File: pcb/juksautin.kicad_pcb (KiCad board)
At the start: 2 copper layers, 65 x 35 mm, 18 parts, among them J1 Screw_Terminal_01x09, J2 ATMEGA32U4 pin 42, U1 SP3485CN, U2 LM4041

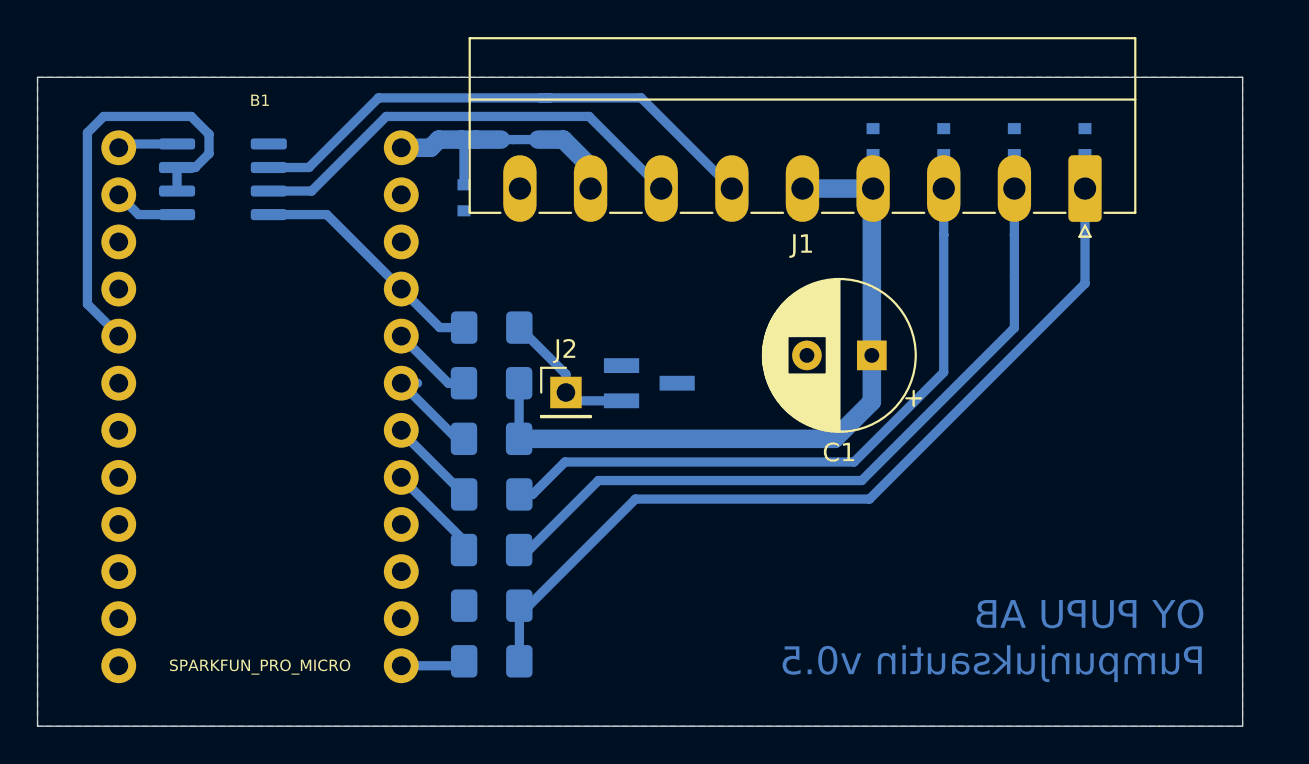
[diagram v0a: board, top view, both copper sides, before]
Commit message: Support 24VDC input
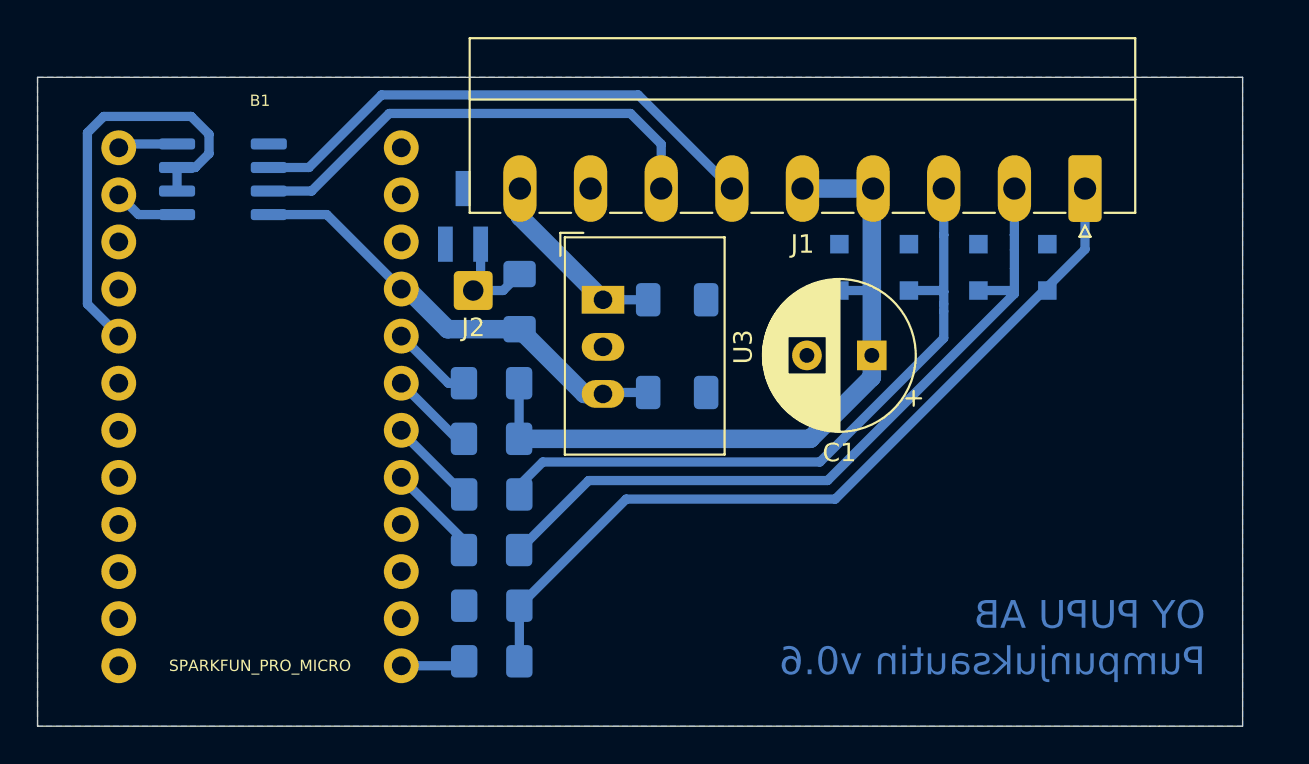
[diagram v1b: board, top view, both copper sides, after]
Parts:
- removed D5: ESD5Z12T1G, Diode_SMD:D_SOD-523
- added C2: 10u, Capacitor_SMD:C_1206_3216Metric_Pad1.33x1.80mm_HandSolder, B.Cu at (144.5, 82.0)
- added C3: 10u, Capacitor_SMD:C_1206_3216Metric_Pad1.33x1.80mm_HandSolder, B.Cu at (144.5, 77.0)
- added U3: R-78E5.0-0.5, Converter_DCDC:Converter_DCDC_RECOM_R-78E-0.5_THT, F.Cu at (140.5, 77.0)
- D1, D2, D3, D4: value ESD5Z3.3T1G -> SD05.TCT; footprint Diode_SMD:D_SOD-523 -> Diode_SMD:D_SOD-323_HandSoldering
- J2: footprint Connector_PinHeader_2.54mm:PinHeader_1x01_P2.54mm_Vertical -> Connector_Wire:SolderWire-0.5sqmm_1x01_D0.9mm_OD2.1mm
- moved U2 13.5 mm to (132.9, 72.5), turned to 90 degrees
- moved J2 7.43 mm to (133.5, 76.5)
- moved D1 7.08 mm to (164.5, 75.2)
- moved D2 7.05 mm to (160.8, 75.2)
- moved D3 7.04 mm to (157.0, 75.2)
- moved D4 7.02 mm to (153.2, 75.2)
- moved R6 2.05 mm to (136.0, 77.1), turned to 90 degrees
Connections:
- B1 pad 24: VIN -> Net-(B1-Pad24)
- J1 pad 8: VIN -> GND
- J1 pad 9: GND -> VIN
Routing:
- net VCC: track 13.2 -> 24.7 mm
- net PUMPFAIL: track 49.2 -> 44.8 mm
- net VIN: track 14.7 -> 10.8 mm
- net K5: track 41.5 -> 39.2 mm
- net IO2: track 38.9 -> 36.7 mm
- net /AREF: track 7.73 -> 5.53 mm
- net B: track 24.4 -> 26.0 mm
- net DRIVE: track 5.50 -> 4.62 mm
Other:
- board text added: "Pumpunjuksautin v0.6"
- board text removed: "Pumpunjuksautin v0.5"

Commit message: pcb: Make the board two-layer instead of one
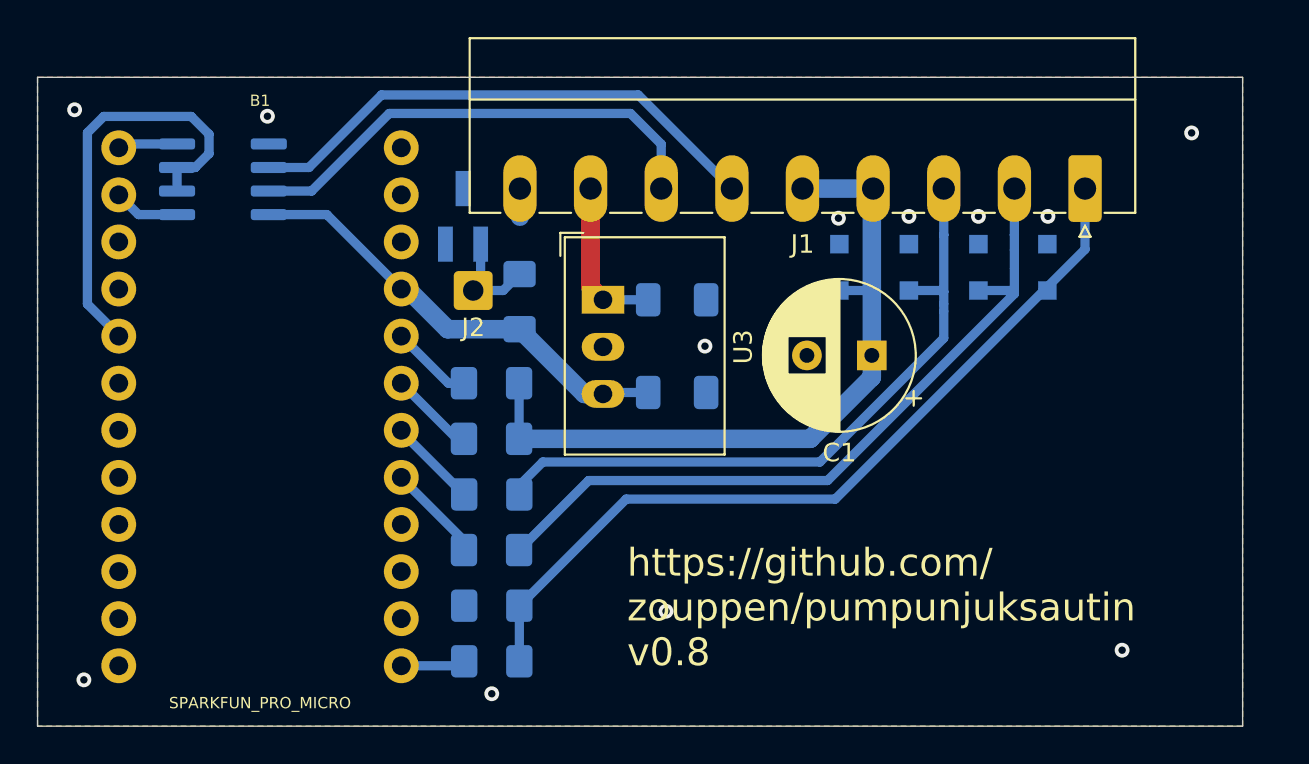
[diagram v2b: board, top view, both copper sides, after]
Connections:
- J1 pad 8: GND -> VIN
- J1 pad 9: VIN -> GND
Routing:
- net VIN: track 10.8 -> 9.22 mm
- net GND: track 0.00 -> 1.52 mm, vias 0 -> 12
- added copper zone on F.Cu, net GND
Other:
- board text added: "0"
- board text added: "1"
- board text added: "2"
- board text added: "A"
- board text added: "B"
- board text added: "https://github.com/ zouppen/pumpunjuksautin v0.8"
- board text added: "⎓"
- board text added: "⏚"
- board text removed: "OY PUPU AB"
- board text removed: "Pumpunjuksautin v0.6"
